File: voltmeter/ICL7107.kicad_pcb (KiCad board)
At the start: 2 copper layers, 88.9 x 68.6 mm, 43 parts, among them J1 +9...12V DC, J2 DP conn., J3 meas. conn, M1 M2.2, M2 M2.2, M3 M2.2, M4 M2.2, U1 LM285Z-1.2, U2 ICL7107, U3 L7805, U4 4069

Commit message: updated file
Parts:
- G1: footprint logo:logo-cc-by-sa-1 -> logo-sq7eqe:cc-by-sa
- renumbered D8 to D2, D9 to D8

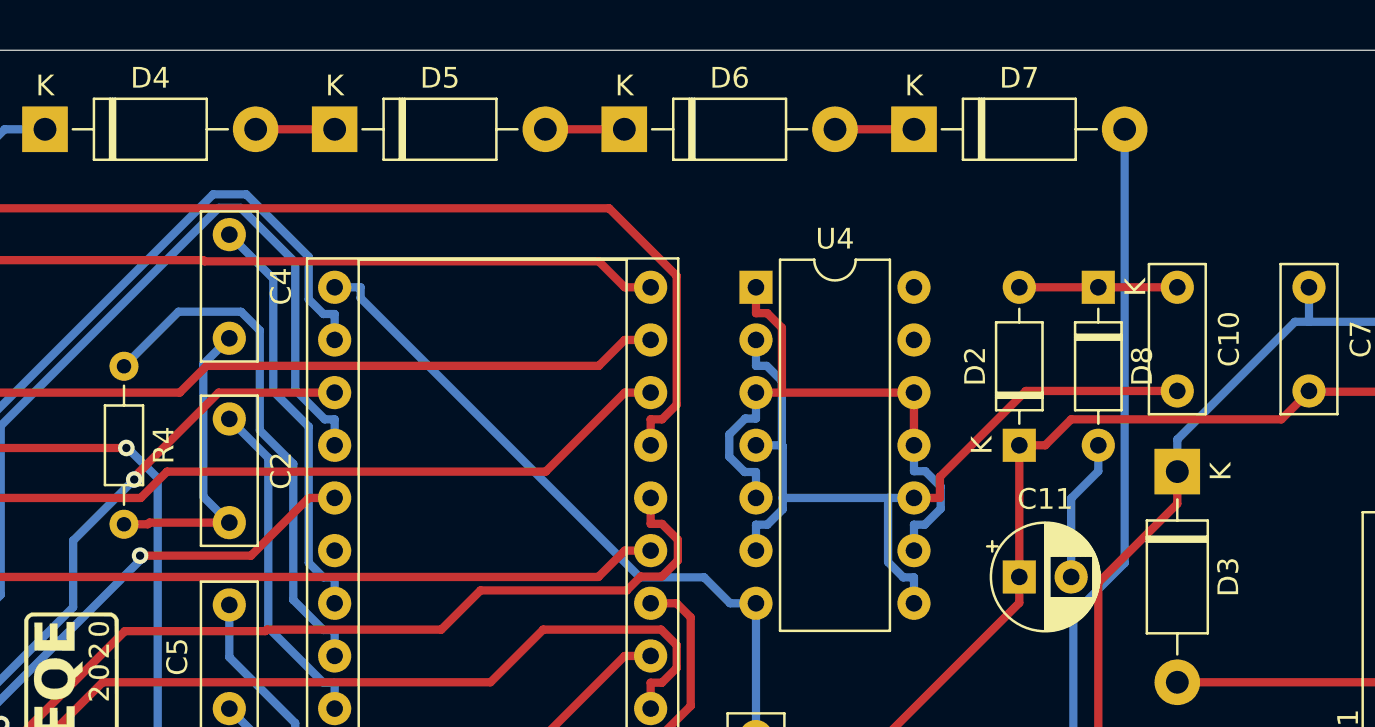
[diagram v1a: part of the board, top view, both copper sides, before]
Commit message: update file
I make mistake in schematics library & footprint library
now devices are correct, I divided 7 segment display at
two separate CA & CC

bye!
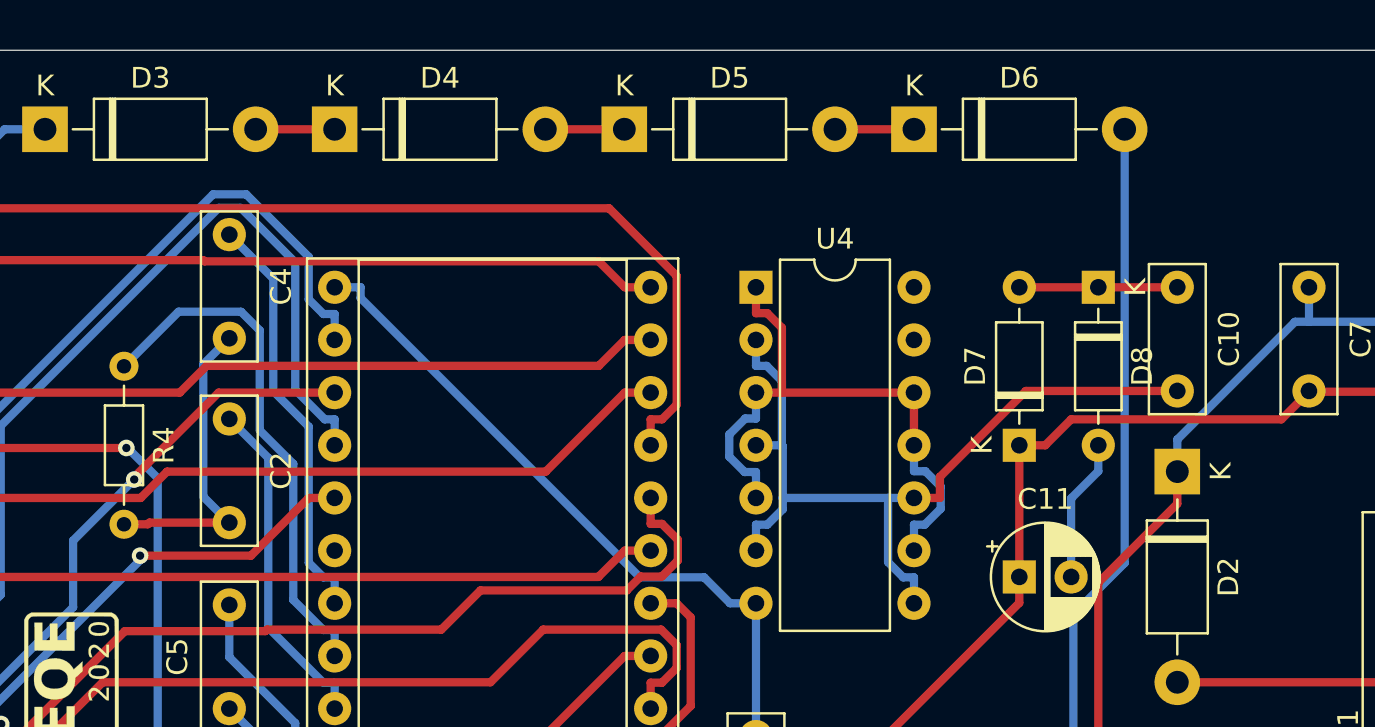
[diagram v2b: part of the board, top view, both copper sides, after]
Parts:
- D1: value LED-Display_x4 -> LED-Display_x4_CA
- renumbered D3 to D2, D4 to D3, D5 to D4, D6 to D5, D7 to D6, D2 to D7

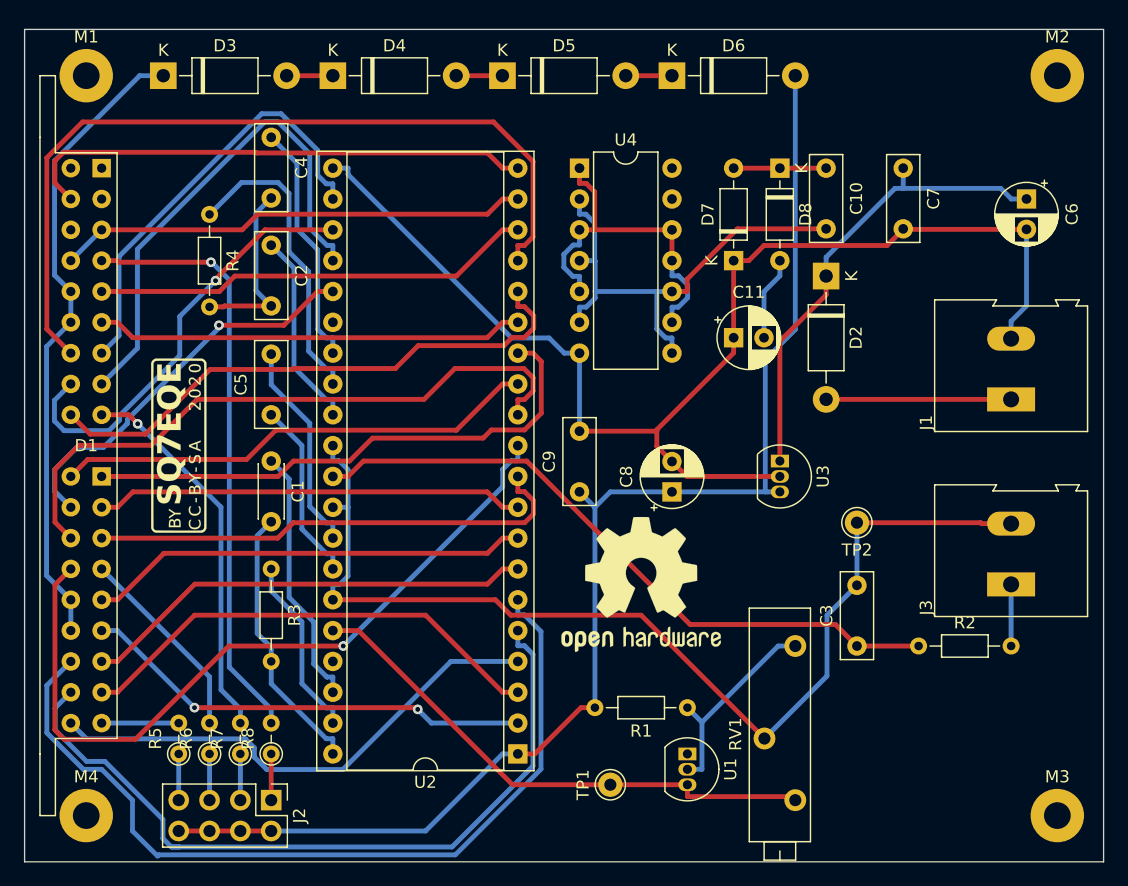
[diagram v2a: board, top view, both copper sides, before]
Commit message: update
Zmodyfikowałem schemat i tym samym projekt płytki drukowanej
usunąłem zbędne rezystory i poprawnie połączyłem dp wyświetlaczy
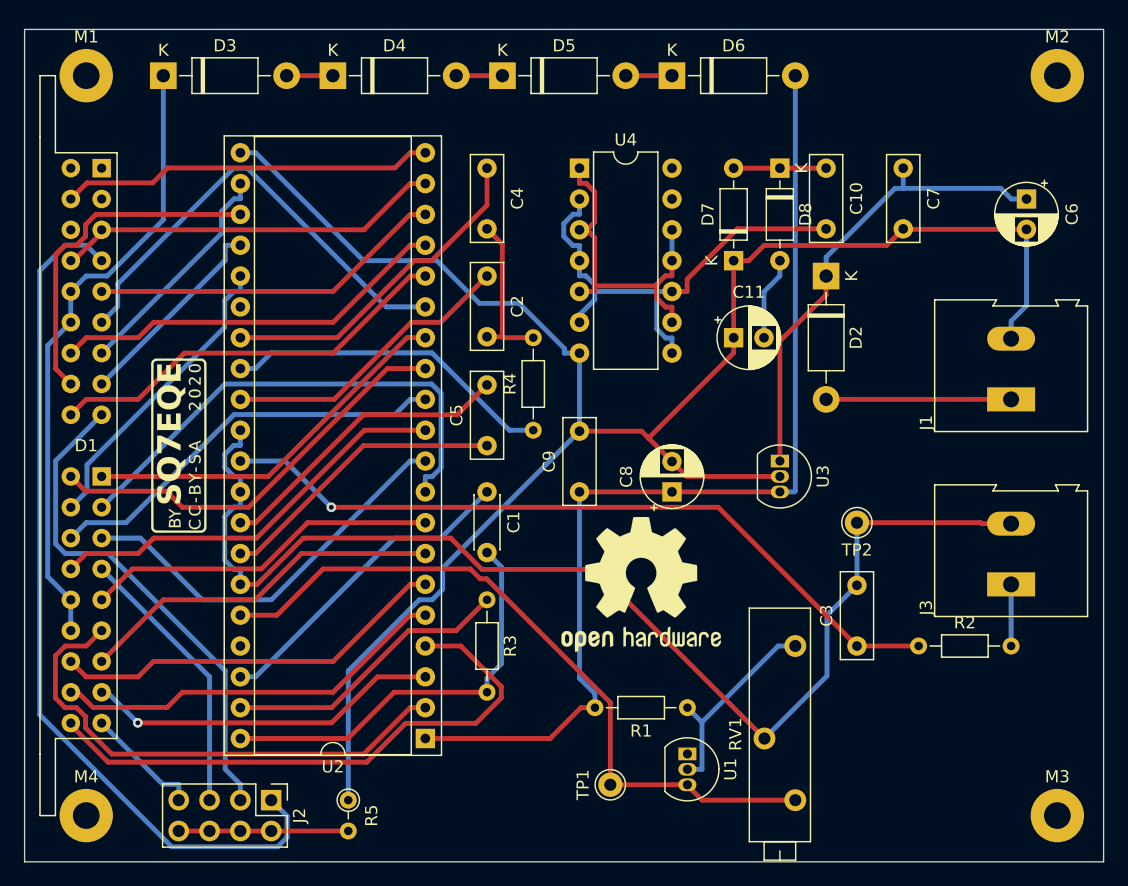
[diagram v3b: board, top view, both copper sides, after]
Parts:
- removed the R5 at (99.1, 119.4)
- removed R6, R7: 470R, Resistor_THT:R_Axial_DIN0204_L3.6mm_D1.6mm_P2.54mm_Vertical
- moved R4 32.1 mm to (128.3, 92.7), turned to 90 degrees
- moved C1 18.0 mm to (124.5, 97.8)
- moved C2 18.0 mm to (124.5, 80.0)
- moved C4 18.0 mm to (124.5, 71.1)
- moved C5 18.0 mm to (124.5, 94.0)
- moved R3 18.0 mm to (124.5, 106.7)
- moved U2 7.73 mm to (119.4, 118.1)
- moved R5 7.41 mm to (113.0, 123.2), turned to 270 degrees
- renumbered R8 to R5
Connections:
- J2 pad 1: Net-(J2-Pad1) -> /DP4
- J2 pad 2: /V+ -> Net-(J2-Pad2)
- J2 pad 3: Net-(J2-Pad3) -> /DP3
- J2 pad 4: /V+ -> Net-(J2-Pad2)
- J2 pad 5: Net-(J2-Pad5) -> /DP2
- J2 pad 6: /V+ -> Net-(J2-Pad2)
- J2 pad 7: Net-(J2-Pad7) -> /DP1
- J2 pad 8: /V+ -> Net-(J2-Pad2)
- R5 pad 1: Net-(J2-Pad1) -> GND
- R5 pad 2: /DP4 -> Net-(J2-Pad2)
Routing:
- net GND: track 103.6 -> 150.7 mm
- net Net-(D1-Pad30): track 71.1 -> 32.9 mm
- net Net-(D1-Pad12): track 68.6 -> 32.9 mm
- net Net-(D1-Pad29): track 63.3 -> 32.9 mm
- net Net-(D1-Pad33): track 63.9 -> 33.9 mm, vias 1 -> 0
- net Net-(D1-Pad8): track 41.9 -> 16.9 mm
- net /DP4: track 49.1 -> 71.9 mm, vias 1 -> 0
- net /V+: track 107.9 -> 85.4 mm
- net Net-(D1-Pad34): track 53.3 -> 33.9 mm
- net Net-(D1-Pad7): track 35.9 -> 19.0 mm
- net Net-(RV1-Pad3): track 44.5 -> 59.2 mm
- net Net-(J2-Pad2): track 0.00 -> 14.0 mm
- net Net-(D1-Pad19): track 44.9 -> 31.4 mm
- net Net-(D1-Pad10): track 46.3 -> 33.9 mm
- net Net-(C1-Pad2): track 22.5 -> 34.4 mm
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
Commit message: update file
poprawiłem schemat i ponownie wygenerowałem pliki Gerber

I corrected the diagram and re-generated the Gerber files
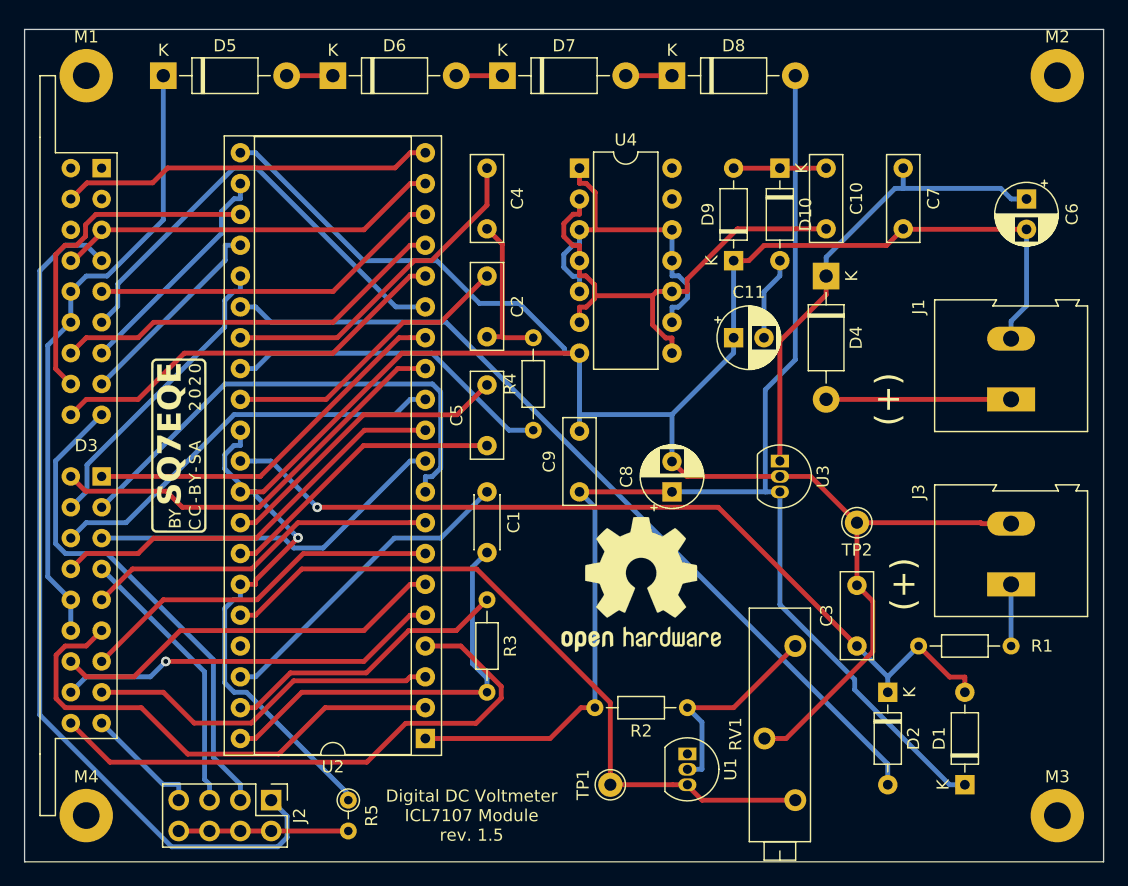
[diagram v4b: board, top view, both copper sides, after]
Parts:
- added D1: 1N4148, Diode_THT:D_DO-35_SOD27_P7.62mm_Horizontal, F.Cu at (163.8, 121.9)
- added D2: 1N4148, Diode_THT:D_DO-35_SOD27_P7.62mm_Horizontal, F.Cu at (157.5, 114.3)
- renumbered D8 to D10, D1 to D3, D2 to D4, D3 to D5, D4 to D6, D5 to D7, D6 to D8, D7 to D9, R2 to R1, R1 to R2
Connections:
- C3 pad 2: /IN- -> GND
- J3 pad 2: /IN- -> GND
- RV1 pad 2: /IN- -> GND
- TP2 pad 1: /IN- -> GND
- U2 pad 30: /IN- -> GND
- U2 pad 32: /IN- -> GND
- U2 pad 35: /IN- -> GND
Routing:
- net /IN-: track 101.4 -> 0.00 mm
- net GND: track 150.7 -> 231.2 mm, vias 0 -> 1
- net /V-: track 0.00 -> 70.6 mm
- net /V+: track 85.4 -> 116.3 mm
- net Net-(C3-Pad1): track 62.2 -> 71.7 mm
- net Net-(D3-Pad21): track 33.5 -> 30.0 mm
- net Net-(U4-Pad1): track 27.8 -> 29.6 mm
- net Net-(D3-Pad29): track 32.9 -> 31.8 mm, vias 0 -> 1
- net Net-(R2-Pad1): track 17.1 -> 17.8 mm
- net Net-(D3-Pad24): track 42.7 -> 42.1 mm
- net Net-(D3-Pad26): vias 1 -> 0
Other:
- board text added: "(+)"
- board text added: "Digital DC Voltmeter ICL7107 Module rev. 1.5"
